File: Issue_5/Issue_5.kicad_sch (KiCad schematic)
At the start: 297 parts, among them IC1 4164A, IC10 4164A, IC11 4164A, IC12 4164A, IC13 4164A, IC14 4164A, IC15 4164A, IC16 4164A, IC17 74LS00, IC18 68008D, IC19 74LS257, IC2 4164A, IC20 74LS257, IC21 74LS245, IC22 ZX8301, IC23 ZX8302, IC24 8749, IC25 MC1488, IC26 MC1489, IC27 74LS03, IC28 MC1377P, IC29 2G007, IC3 4164A, IC30 2G007, IC31 LM7805_TO220, IC32 LM7805_TO220, IC33 27256, IC34 27128, IC36 L7912, IC37 L7812, IC4 4164A, IC5 4164A, IC6 4164A, IC7 4164A, IC8 4164A, IC9 4164A, J1 QL_SLOT_DIN41612, J10 AudioJack2_Ground_Switch, J101 Conn_01x07, J102 Conn_01x07, J11 Conn_01x09_Socket, J12 Conn_01x11_Socket, J2 QL_cartridge_ROM, J201 Conn_01x07, J202 Conn_01x07, J3 Conn_01x06, J4 Conn_01x06, J5 Conn_01x06, J6 Conn_01x06, J7 DIN-8, J8 Conn_01x03_Pin, J9 AudioJack2_Ground_Switch, M1 UM1233, M2 Motor_DC, M3 Motor_DC, SW1 SW_SPDT, SW2 SW_SPDT, U35 LM7805_TO220, X1 15Mhz, X2 32768Khz, X3 4.4336Mhz, X4 11Mhz

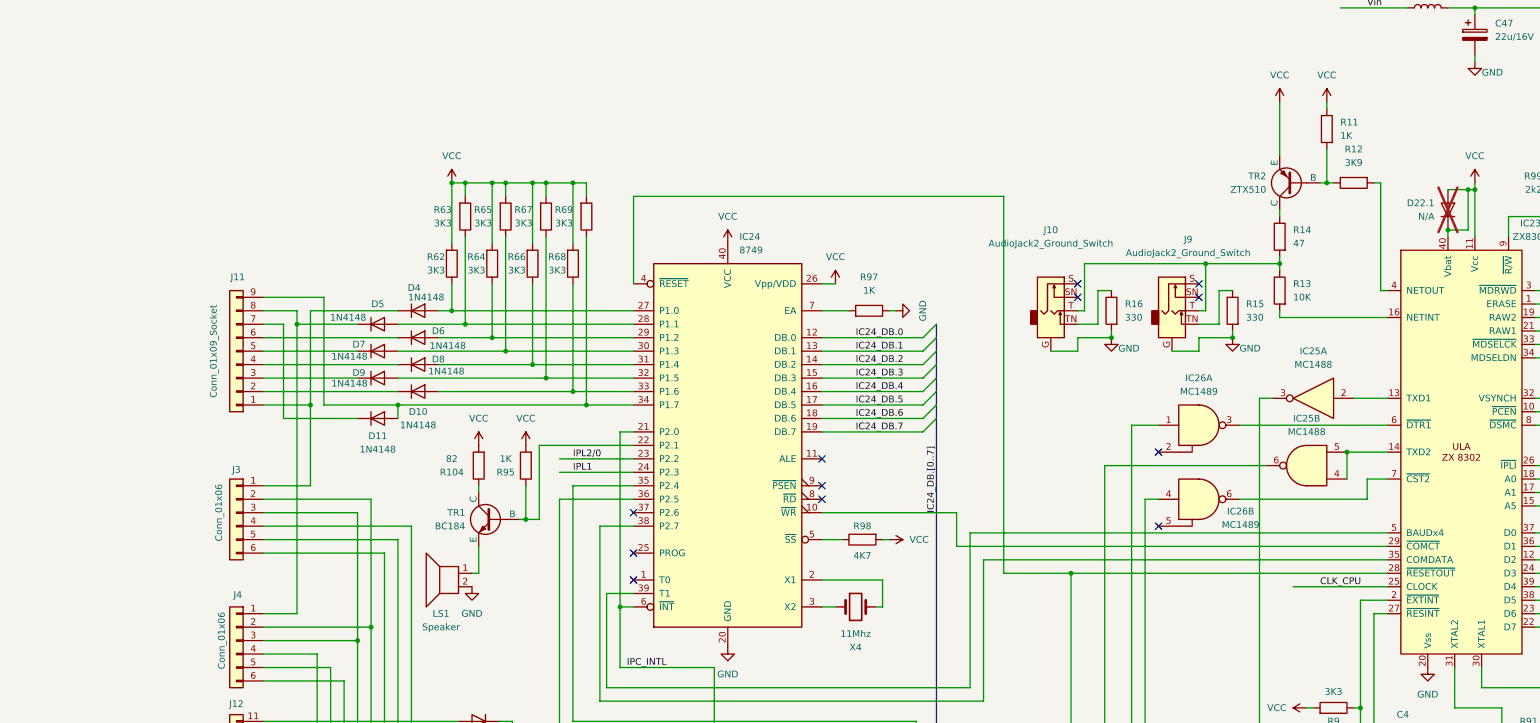
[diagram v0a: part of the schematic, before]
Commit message: small fix on Issue 5
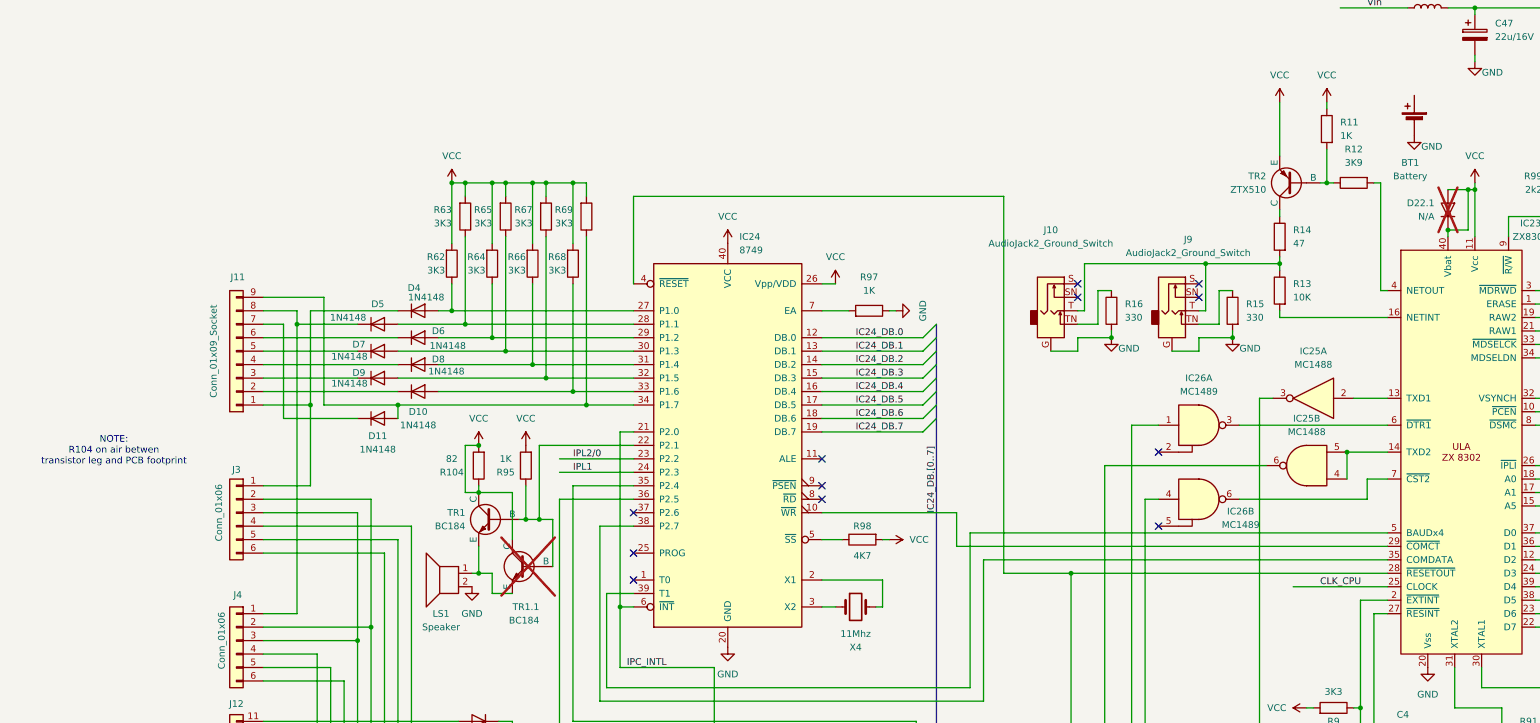
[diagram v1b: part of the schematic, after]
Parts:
- added BT1: Battery, Connector_PinSocket_2.54mm:PinSocket_1x02_P2.54mm_Vertical, symbol Device:Battery_Cell
- added TR1.1: BC184, 8bits:TO-92-SINCLAIR, symbol Simulation_SPICE:NPN
- TC1: footprint Capacitor_THT:C_Radial_D10.0mm_H12.5mm_P5.00mm -> Capacitor_THT:C_Radial_D16.0mm_H25.0mm_P7.50mm
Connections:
- net GND: now also BT1.2 (-)
- net VCC: now also R104.1, TR1.1 (C), TR1.1.1 (C)
- net at IC24.22 (P2.1), R95.1, TR1.2 (B): now also TR1.1.2 (B)
- net at LS1.1, TR1.3 (E): now also TR1.1.3 (E)
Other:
- note added: "NOTE: R104 on air betwen transistor leg and PCB footprint"

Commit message: small updates to issue 5
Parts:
- removed D22.1: N/A, 8bits:D_DO-34_SOD68_P12.7mm_Horizontal, symbol Device:D
- removed R102, R103: 0, 8bits:R_Axial_DIN0207_L6.3mm_D2.5mm_P12.7mm_Horizontal_W, symbol Device:R
- added D22, D23: 1N4148, 8bits:D_DO-34_SOD68_P12.7mm_Horizontal, symbol Device:D
- added R81, R82, R83, R84: N.P., 8bits:R_Axial_DIN0207_L6.3mm_D2.5mm_P12.7mm_Horizontal_W, symbol Device:R
- added Z2: N.P., 8bits:D_DO-34_SOD68_P12.7mm_Horizontal, symbol Device:D
- D29: footprint 8bits:D_DO-34_SOD68_P12.7mm_Horizontal -> 8bits:D_DO-34_SOD68_P7.62mm_Horizontal_45deg
- R47: value 1K -> 2K2
- TC1: footprint Capacitor_THT:C_Radial_D16.0mm_H25.0mm_P7.50mm -> 8bits:C_ajustable
- renumbered D22 to D22-1, D23 to D23-2, R107 to R102, R108 to R103
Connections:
- net GND: now also R84.1, Z2.2 (A)
- net RAW1: now also IC23.21 (RAW1)
- net RAW2: now also IC23.19 (RAW2)
- net VCC: now also IC27.12, D23.2 (A), R81.1; no longer DC6.1, IC23.40 (Vbat), IC27.13, TR1.1.1 (C)
- net Vin: now also TR1.1.3 (E), R82.2
- net at IC24.22 (P2.1), R95.1, TR1.1.2 (B)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: now also R81.2, R82.1
- net at IC27.8, R93.1: now also IC27.13; no longer IC27.12
- net at LS1.1, TR1.3 (E): no longer TR1.1.3 (E)
- net IC23_3: now reaches IC23.3 (~{MDRWD}), R99.1
- net IC23_3: now also R83.1, R84.2, Z2.1 (K)
- net at J5.6 (Pin_6), J6.6 (Pin_6), R10.2: no longer IC25.8, J6.5 (Pin_5)
- net EA: now reaches IC24.7 (EA), R97.2
- net at BT1.1 (+): now also D22.2 (A)
- new net: D22.1 (K), D23.1 (K), DC6.1, IC23.40 (Vbat)
- new net: R83.2, TR1.1.1 (C)
- new net: IC25.8, J6.5 (Pin_5)
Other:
- note added: "NOTE: R102,R103 Aereal instalation over IC23 an a wire to -12V (PIN 1 of IC25)"
- note added: "NOTE: Service Manual Mandatory Update R106 Aereal instalation over C19"
- note added: "NOTE: Service Manual Mandatory Update R106 Aereal instalation over D17 in solder side"
- note removed: "NOTE: R107,R108 Aereal instalation over IC23 an a wire to -12V (PIN 1 of IC25)"
- moved on the sheet: BT1, C47, D10, D11, D29, D4, D5, D6, D7, D8, D9, DC6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
